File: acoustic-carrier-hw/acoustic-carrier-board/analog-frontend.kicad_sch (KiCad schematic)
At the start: 96 parts, among them J1001 BWU.FL-IPEX1, J1002 BWU.FL-IPEX1, J1003 BWU.FL-IPEX1, J1004 BWU.FL-IPEX1, J1005 BWU.FL-IPEX1, J1006 BWU.FL-IPEX1, J1007 8P8C_Shielded, J1008 BWU.FL-IPEX1, U1001 MS9280, U1002 THS4521IDGK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

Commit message: [carrier] Removed USB-switch, placed decouplpling for DDR3 and ECP5U (next) consider adding buffers on CC1 and CC2 pins
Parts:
- C1002, C1003, C1004, C1005, C1008, C1010, C1013, C1019, C1021: footprint Capacitor_SMD:C_0402_1005Metric -> Capacitor_SMD:C_0201_0603Metric; LPN C307331 -> C22435929; MPN CL05B104KB54PNC -> CGA0201X7R104K160ET
- C1011: footprint Capacitor_SMD:C_0402_1005Metric -> Capacitor_SMD:C_0201_0603Metric; LPN C15195 -> C285010; MPN CL05B103KB5NNNC -> 0201B103K250NT
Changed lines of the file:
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@@
 			)
 		)
-		(property "Footprint" "Capacitor_SMD:C_0402_1005Metric"
+		(property "Footprint" "Capacitor_SMD:C_0201_0603Metric"
 			(at 370.84 57.15 0)
 			(effects
@@
 			)
 		)
-		(property "Datasheet" "https://jlcpcb.com/api/file/downloadByFileSystemAccessId/8554627388281098240"
+		(property "Datasheet" "https://jlcpcb.com/api/file/downloadByFileSystemAccessId/8603345729432014848"
 			(at 370.84 57.15 0)
 			(effects
@@
 			)
 		)
-		(property "LPN" "C307331"
+		(property "LPN" "C22435929"
 			(at 370.84 57.15 0)
 			(effects
@@
 			)
 		)
-		(property "MPN" "CL05B104KB54PNC"
+		(property "MPN" "CGA0201X7R104K160ET "
 			(at 370.84 57.15 0)
 			(effects
@@
 			)
 		)
-		(property "Footprint" "Capacitor_SMD:C_0402_1005Metric"
+		(property "Footprint" "Capacitor_SMD:C_0201_0603Metric"
 			(at 372.11 31.75 0)
 			(effects
@@
 			)
 		)
-		(property "Datasheet" "~"
+		(property "Datasheet" "https://jlcpcb.com/api/file/downloadByFileSystemAccessId/8603345729432014848"
 			(at 372.11 31.75 0)
 			(effects
@@
 			)
 		)
-		(property "LPN" "C307331"
+		(property "LPN" "C22435929"
 			(at 372.11 31.75 0)
 			(effects
@@
 			)
 		)
-		(property "MPN" "CL05B104KB54PNC"
+		(property "MPN" "CGA0201X7R104K160ET "
 			(at 372.11 31.75 0)
 			(effects
@@
 			)
 		)
-		(property "Footprint" "Capacitor_SMD:C_0402_1005Metric"
+		(property "Footprint" "Capacitor_SMD:C_0201_0603Metric"
 			(at 382.27 31.75 0)
 			(effects
@@
 			)
 		)
-		(property "Datasheet" "~"
+		(property "Datasheet" "https://jlcpcb.com/api/file/downloadByFileSystemAccessId/8603345729432014848"
 			(at 382.27 31.75 0)
 			(effects
@@
 			)
 		)
-		(property "LPN" "C307331"
+		(property "LPN" "C22435929"
 			(at 382.27 31.75 0)
 			(effects
@@
 			)
 		)
-		(property "MPN" "CL05B104KB54PNC"
+		(property "MPN" "CGA0201X7R104K160ET "
 			(at 382.27 31.75 0)
 			(effects
@@
 			)
 		)
-		(property "Footprint" "Capacitor_SMD:C_0402_1005Metric"
+		(property "Footprint" "Capacitor_SMD:C_0201_0603Metric"
 			(at 298.45 78.74 0)
 			(effects
@@
 			)
 		)
-		(property "Datasheet" "~"
+		(property "Datasheet" "https://jlcpcb.com/api/file/downloadByFileSystemAccessId/8603345729432014848"
 			(at 298.45 78.74 0)
 			(effects
@@
 			)
 		)
-		(property "LPN" "C307331"
+		(property "LPN" "C22435929"
 			(at 298.45 78.74 0)
 			(effects
@@
 			)
 		)
-		(property "MPN" "CL05B104KB54PNC"
+		(property "MPN" "CGA0201X7R104K160ET "
 			(at 298.45 78.74 0)
 			(effects
@@
 			)
 		)
-		(property "Footprint" "Capacitor_SMD:C_0402_1005Metric"
+		(property "Footprint" "Capacitor_SMD:C_0201_0603Metric"
 			(at 196.85 69.85 0)
 			(effects
@@
 			)
 		)
-		(property "Datasheet" "https://jlcpcb.com/api/file/downloadByFileSystemAccessId/8579707307011465216"
+		(property "Datasheet" "https://jlcpcb.com/api/file/downloadByFileSystemAccessId/8589040499521306624"
 			(at 196.85 69.85 0)
 			(effects
@@
 			)
 		)
-		(property "LPN" "C15195"
+		(property "LPN" "C285010"
 			(at 196.85 69.85 0)
 			(effects
@@
 			)
 		)
-		(property "MPN" "CL05B103KB5NNNC"
+		(property "MPN" "0201B103K250NT"
 			(at 196.85 69.85 0)
 			(effects
@@
 			)
 		)
-		(property "Footprint" "Capacitor_SMD:C_0402_1005Metric"
+		(property "Footprint" "Capacitor_SMD:C_0201_0603Metric"
 			(at 144.78 246.38 0)
 			(effects
@@
 			)
 		)
-		(property "Datasheet" "~"
+		(property "Datasheet" "https://jlcpcb.com/api/file/downloadByFileSystemAccessId/8603345729432014848"
 			(at 144.78 246.38 0)
 			(effects
@@
 			)
 		)
-		(property "LPN" "C307331"
+		(property "LPN" "C22435929"
 			(at 144.78 246.38 0)
 			(effects
@@
 			)
 		)
-		(property "MPN" "CL05B104KB54PNC"
+		(property "MPN" "CGA0201X7R104K160ET "
 			(at 144.78 246.38 0)
 			(effects
@@
 			)
 		)
-		(property "Footprint" "Capacitor_SMD:C_0402_1005Metric"
+		(property "Footprint" "Capacitor_SMD:C_0201_0603Metric"
 			(at 337.82 57.15 0)
 			(effects
@@
 			)
 		)
-		(property "Datasheet" "~"
+		(property "Datasheet" "https://jlcpcb.com/api/file/downloadByFileSystemAccessId/8603345729432014848"
 			(at 337.82 57.15 0)
 			(effects
@@
 			)
 		)
-		(property "LPN" "C307331"
+		(property "LPN" "C22435929"
 			(at 337.82 57.15 0)
 			(effects
@@
 			)
 		)
-		(property "MPN" "CL05B104KB54PNC"
+		(property "MPN" "CGA0201X7R104K160ET "
 			(at 337.82 57.15 0)
 			(effects
@@
 			)
 		)
-		(property "Footprint" "Capacitor_SMD:C_0402_1005Metric"
+		(property "Footprint" "Capacitor_SMD:C_0201_0603Metric"
 			(at 191.77 69.85 0)
 			(effects
@@
 			)
 		)
-		(property "Datasheet" "~"
+		(property "Datasheet" "https://jlcpcb.com/api/file/downloadByFileSystemAccessId/8603345729432014848"
 			(at 191.77 69.85 0)
 			(effects
@@
 			)
 		)
-		(property "LPN" "C307331"
+		(property "LPN" "C22435929"
 			(at 191.77 69.85 0)
 			(effects
@@
 			)
 		)
-		(property "MPN" "CL05B104KB54PNC"
+		(property "MPN" "CGA0201X7R104K160ET "
 			(at 191.77 69.85 0)
 			(effects
@@
 			)
 		)
-		(property "Footprint" "Capacitor_SMD:C_0402_1005Metric"
+		(property "Footprint" "Capacitor_SMD:C_0201_0603Metric"
 			(at 86.36 73.66 0)
 			(effects
@@
 			)
 		)
-		(property "Datasheet" "~"
+		(property "Datasheet" "https://jlcpcb.com/api/file/downloadByFileSystemAccessId/8603345729432014848"
 			(at 86.36 73.66 0)
 			(effects
@@
 			)
 		)
-		(property "LPN" "C307331"
+		(property "LPN" "C22435929"
 			(at 86.36 73.66 0)
 			(effects
@@
 			)
 		)
-		(property "MPN" "CL05B104KB54PNC"
+		(property "MPN" "CGA0201X7R104K160ET "
 			(at 86.36 73.66 0)
 			(effects
@@
 			)
 		)
-		(property "Footprint" "Capacitor_SMD:C_0402_1005Metric"
+		(property "Footprint" "Capacitor_SMD:C_0201_0603Metric"
 			(at 391.16 26.67 0)
 			(effects
@@
 			)
 		)
-		(property "Datasheet" "~"
+		(property "Datasheet" "https://jlcpcb.com/api/file/downloadByFileSystemAccessId/8603345729432014848"
 			(at 391.16 26.67 0)
 			(effects
@@
 			)
 		)
-		(property "LPN" "C307331"
+		(property "LPN" "C22435929"
 			(at 391.16 26.67 0)
 			(effects
@@
 			)
 		)
-		(property "MPN" "CL05B104KB54PNC"
+		(property "MPN" "CGA0201X7R104K160ET "
 			(at 391.16 26.67 0)
 			(effects

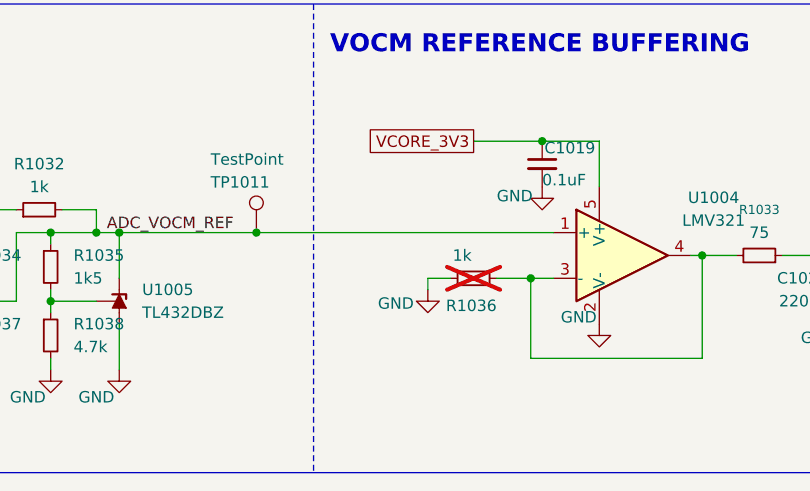
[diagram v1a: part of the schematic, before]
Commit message: [¢arrier] Placed decoupling for some banks, placed dc-dc converterss (next) switch dc-dc converter pins around, switch adc-inputs around
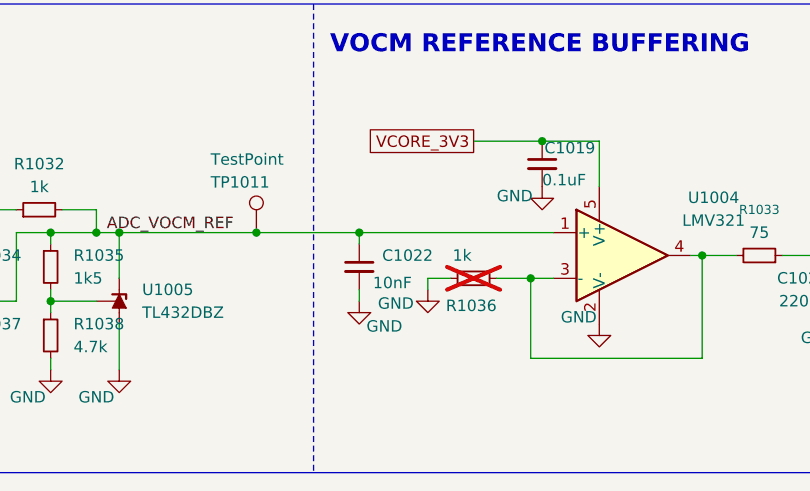
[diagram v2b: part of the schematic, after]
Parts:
- added C1022: 10nF, Capacitor_SMD:C_0201_0603Metric, symbol Device:C_Small
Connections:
- net ADC_VOCM_REF: now also C1022.1
- net GND: now also C1022.2

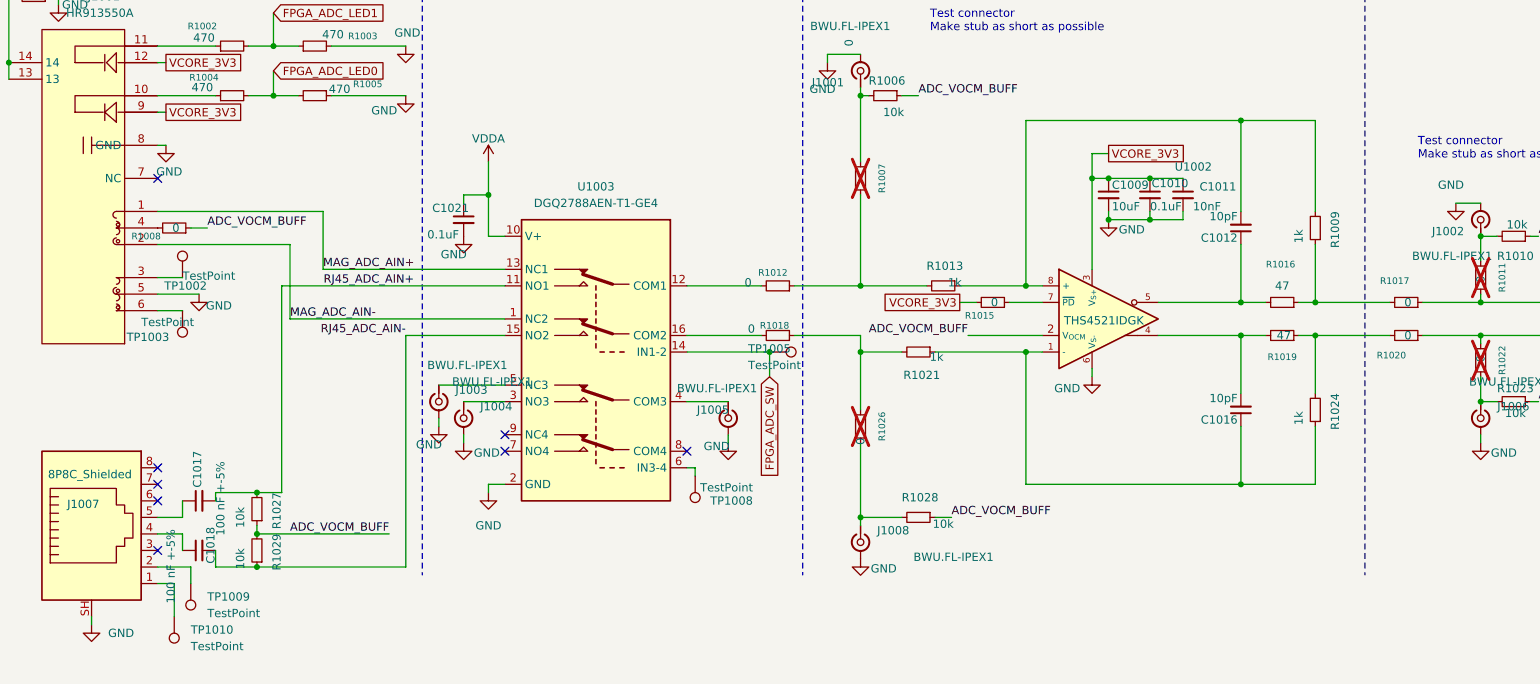
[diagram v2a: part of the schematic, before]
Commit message: [carrier] Rearanged big parts of the analog PCB
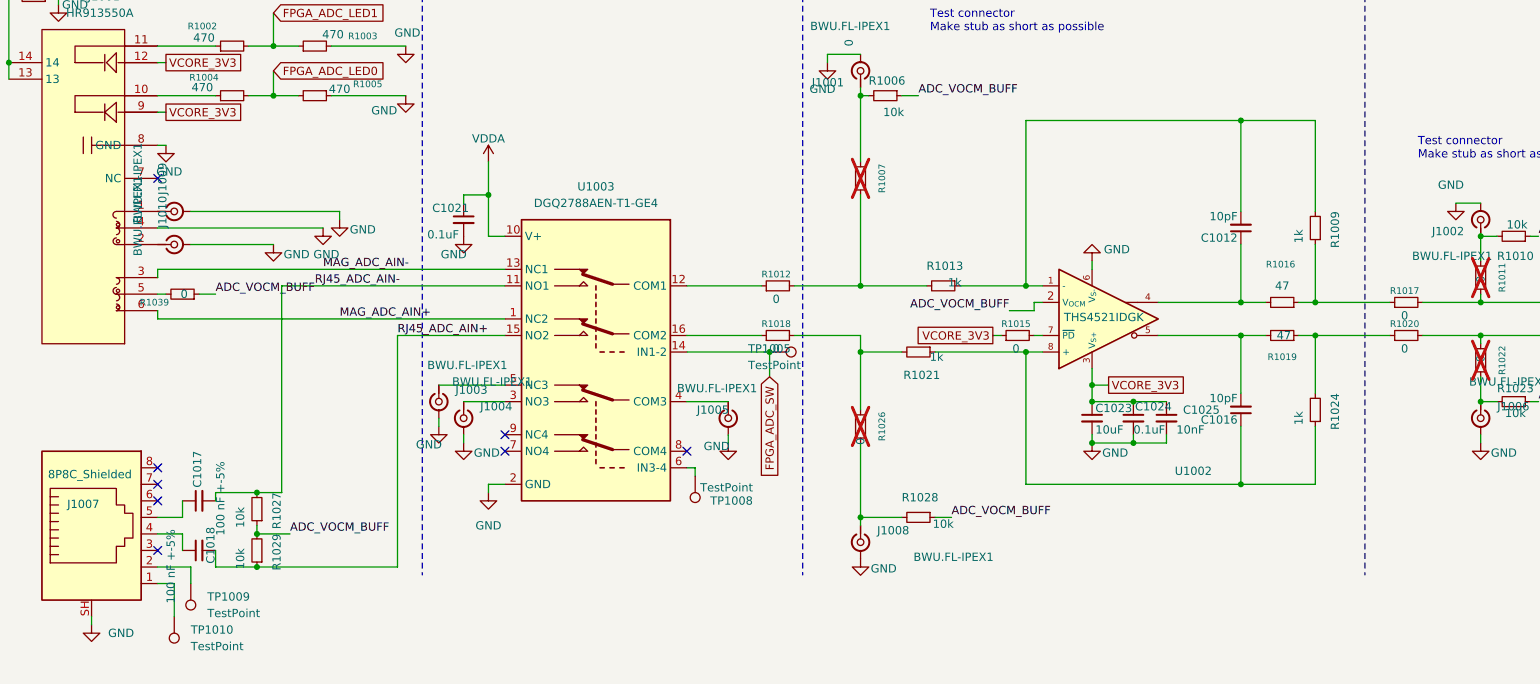
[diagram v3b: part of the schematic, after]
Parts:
- removed C1009: 10uF, Capacitor_SMD:C_0603_1608Metric, symbol Device:C_Small
- removed C1010: 0.1uF, Capacitor_SMD:C_0201_0603Metric, symbol Device:C_Small
- removed C1011: 10nF, Capacitor_SMD:C_0201_0603Metric, symbol Device:C_Small
- removed R1008: 0, Resistor_SMD:R_0603_1608Metric, symbol Device:R_Small
- removed TP1002, TP1003: TestPoint, TestPoint:TestPoint_Loop_D1.80mm_Drill1.0mm_Beaded, symbol Connector:TestPoint
- added C1023: 10uF, Capacitor_SMD:C_0603_1608Metric, symbol Device:C_Small
- added C1024: 0.1uF, Capacitor_SMD:C_0201_0603Metric, symbol Device:C_Small
- added C1025: 10nF, Capacitor_SMD:C_0201_0603Metric, symbol Device:C_Small
- added J1009, J1010: BWU.FL-IPEX1, iw-connector:BWU.FL-IPEX1, symbol Connector:Conn_Coaxial_Small
- added R1039: 0, Resistor_SMD:R_0603_1608Metric, symbol Device:R_Small
- R1012, R1015, R1017, R1018, R1020: footprint Resistor_SMD:R_0603_1608Metric -> Resistor_SMD:R_0402_1005Metric_Pad0.72x0.64mm_HandSolder; LPN C21189 -> C17168; MPN 0603WAF0000T5E -> 0402WGF0000TCE
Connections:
- net ADC_AIN+: now also R1017.2; no longer R1017.1
- net ADC_AIN-: now also R1020.2; no longer R1020.1
- net ADC_VOCM_BUFF: now also R1039.1
- net GND: now also RJ1001.4, C1023.2, C1024.2, C1025.2, J1009.2 (Ext), J1010.2 (Ext); no longer RJ1001.5
- net MAG_ADC_AIN+: now also RJ1001.6, U1003.1 (NC2); no longer RJ1001.1, U1003.13 (NC1)
- net MAG_ADC_AIN-: now also RJ1001.3, U1003.13 (NC1); no longer RJ1001.2, U1003.1 (NC2)
- net RJ45_ADC_AIN+: now also C1018.2, R1029.1, U1003.15 (NO2); no longer C1017.2, R1027.2, U1003.11 (NO1)
- net RJ45_ADC_AIN-: now also C1017.2, R1027.2, U1003.11 (NO1); no longer C1018.2, R1029.1, U1003.15 (NO2)
- net VCORE_3V3: now also R1015.1, C1023.1, C1024.1, C1025.1; no longer R1015.2
- net at R1007.2, R1013.2: now also R1012.2; no longer R1012.1
- net at U1003.12 (COM1): now also R1012.1; no longer R1012.2
- net at C1016.1, R1021.1, R1024.1: now also U1002.8 (+); no longer U1002.1 (-)
- net at C1016.2, R1019.2: now also U1002.5; no longer U1002.4
- net at C1012.1, R1016.2: now also U1002.4; no longer U1002.5
- net at U1002.7 (~{PD}): now also R1015.2; no longer R1015.1
- net at C1012.2, R1009.2, R1013.1: now also U1002.1 (-); no longer U1002.8 (+)
- net at R1021.2, R1026.1: now also R1018.2; no longer R1018.1
- net at U1003.16 (COM2): now also R1018.1; no longer R1018.2
- net at R1009.1, R1016.1: now also R1017.1; no longer R1017.2
- net at R1019.1, R1024.2: now also R1020.1; no longer R1020.2
- new net: J1009.1 (In), RJ1001.1
- new net: J1010.1 (In), RJ1001.2
- new net: R1039.2, RJ1001.5
